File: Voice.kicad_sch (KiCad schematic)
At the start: 11 parts, among them Q401 MMBT3904, Q402 BSS84, U401 NE555D

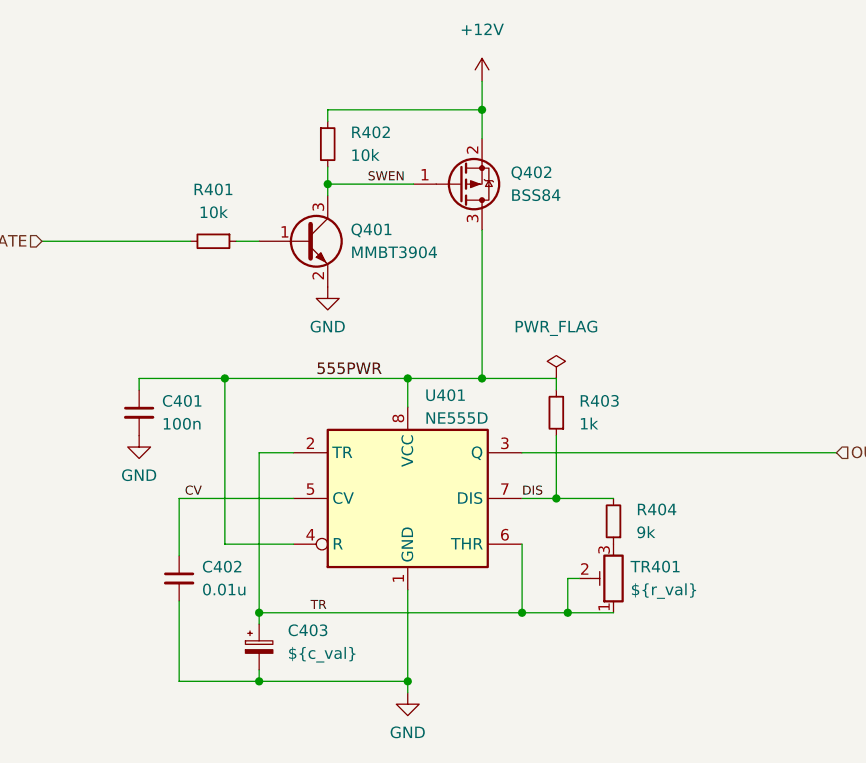
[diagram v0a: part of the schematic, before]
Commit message: swap to SMD Bourns 3224W, can stack in Eurorack now
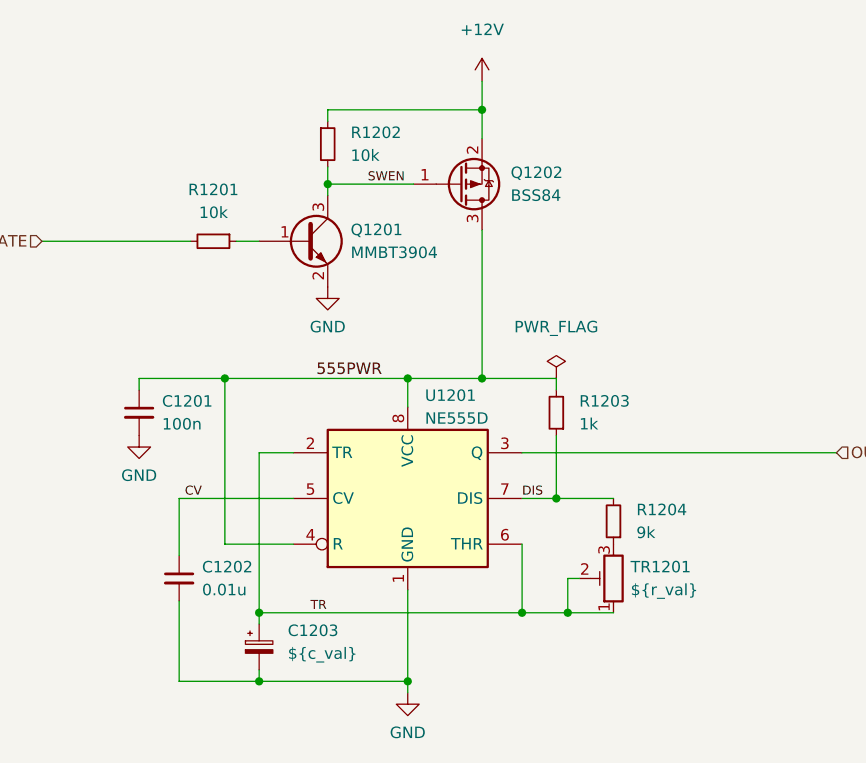
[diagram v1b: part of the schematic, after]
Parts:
- TR1201: renamed from TR401; footprint Potentiometer_THT:Potentiometer_Bourns_3296W_Vertical -> TripleFiveSynth:Potentiometer_Bourns_3224W_Vertical
- renumbered C401 to C1201, C402 to C1202, C403 to C1203, Q401 to Q1201, Q402 to Q1202, R401 to R1201, R402 to R1202, R403 to R1203, R404 to R1204, U401 to U1201
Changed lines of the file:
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@@
   (symbol (lib_id "Device:R_Potentiometer_Trim") (at 144.145 104.14 180)
     (in_bom yes) (on_board yes) (fields_autoplaced)
-    (property "Reference" "TR401" (id 0) (at 146.05 102.8699 0)
+    (property "Reference" "TR1201" (id 0) (at 146.05 102.8699 0)
       (effects (font (size 1.27 1.27)) (justify right))
     )
@@
       (effects (font (size 1.27 1.27)) (justify right))
     )
-    (property "Footprint" "Potentiometer_THT:Potentiometer_Bourns_3296W_Vertical" (id 2) (at 144.145 104.14 0)
+    (property "Footprint" "TripleFiveSynth:Potentiometer_Bourns_3224W_Vertical" (id 2) (at 144.145 104.14 0)
       (effects (font (size 1.27 1.27)) hide)
     )
@@
   (symbol (lib_id "Transistor_BJT:MMBT3904") (at 109.855 66.675 0)
     (in_bom yes) (on_board yes) (fields_autoplaced)
-    (property "Reference" "Q401" (id 0) (at 114.935 65.4049 0)
+    (property "Reference" "Q1201" (id 0) (at 114.935 65.4049 0)
       (effects (font (size 1.27 1.27)) (justify left))
     )
@@
   (symbol (lib_id "Timer:NE555D") (at 121.285 95.25 0)
     (in_bom yes) (on_board yes)
-    (property "Reference" "U401" (id 0) (at 123.19 83.82 0)
+    (property "Reference" "U1201" (id 0) (at 123.19 83.82 0)
       (effects (font (size 1.27 1.27)) (justify left))
     )
@@
   (symbol (lib_id "Device:C_Small") (at 95.885 104.14 0)
     (in_bom yes) (on_board yes) (fields_autoplaced)
-    (property "Reference" "C402" (id 0) (at 98.425 102.8762 0)
+    (property "Reference" "C1202" (id 0) (at 98.425 102.8762 0)
       (effects (font (size 1.27 1.27)) (justify left))
     )
@@
   (symbol (lib_id "Device:C_Small") (at 91.44 85.725 0)
     (in_bom yes) (on_board yes) (fields_autoplaced)
-    (property "Reference" "C401" (id 0) (at 93.98 84.4612 0)
+    (property "Reference" "C1201" (id 0) (at 93.98 84.4612 0)
       (effects (font (size 1.27 1.27)) (justify left))
     )
@@
   (symbol (lib_id "Device:R_Small") (at 137.795 85.725 180)
     (in_bom yes) (on_board yes) (fields_autoplaced)
-    (property "Reference" "R403" (id 0) (at 140.335 84.4549 0)
+    (property "Reference" "R1203" (id 0) (at 140.335 84.4549 0)
       (effects (font (size 1.27 1.27)) (justify right))
     )
@@
   (symbol (lib_id "Device:R_Small") (at 112.395 55.88 0)
     (in_bom yes) (on_board yes) (fields_autoplaced)
-    (property "Reference" "R402" (id 0) (at 114.935 54.6099 0)
+    (property "Reference" "R1202" (id 0) (at 114.935 54.6099 0)
       (effects (font (size 1.27 1.27)) (justify left))
     )
@@
   (symbol (lib_id "Device:R_Small") (at 99.695 66.675 270)
     (in_bom yes) (on_board yes) (fields_autoplaced)
-    (property "Reference" "R401" (id 0) (at 99.695 60.96 90))
+    (property "Reference" "R1201" (id 0) (at 99.695 60.96 90))
     (property "Value" "10k" (id 1) (at 99.695 63.5 90))
     (property "Footprint" "Resistor_SMD:R_0603_1608Metric" (id 2) (at 99.695 66.675 0)
@@
   (symbol (lib_id "Transistor_FET:BSS84") (at 127 60.325 0) (mirror x)
     (in_bom yes) (on_board yes) (fields_autoplaced)
-    (property "Reference" "Q402" (id 0) (at 132.715 59.0549 0)
+    (property "Reference" "Q1202" (id 0) (at 132.715 59.0549 0)
       (effects (font (size 1.27 1.27)) (justify left))
     )
@@
   (symbol (lib_id "Device:R_Small") (at 144.145 97.79 180)
     (in_bom yes) (on_board yes) (fields_autoplaced)
-    (property "Reference" "R404" (id 0) (at 146.685 96.5199 0)
+    (property "Reference" "R1204" (id 0) (at 146.685 96.5199 0)
       (effects (font (size 1.27 1.27)) (justify right))
     )
@@
   (symbol (lib_id "Device:C_Polarized_Small") (at 104.775 111.76 0)
     (in_bom yes) (on_board yes) (fields_autoplaced)
-    (property "Reference" "C403" (id 0) (at 107.95 109.9438 0)
-      (effects (font (size 1.27 1.27)) (justify left))
-    )
+    (property "Reference" "C1203" (id 0) (at 107.95 109.9438 0)
+      (effects (font (size 1.27 1.27)) (justify left))
+    )

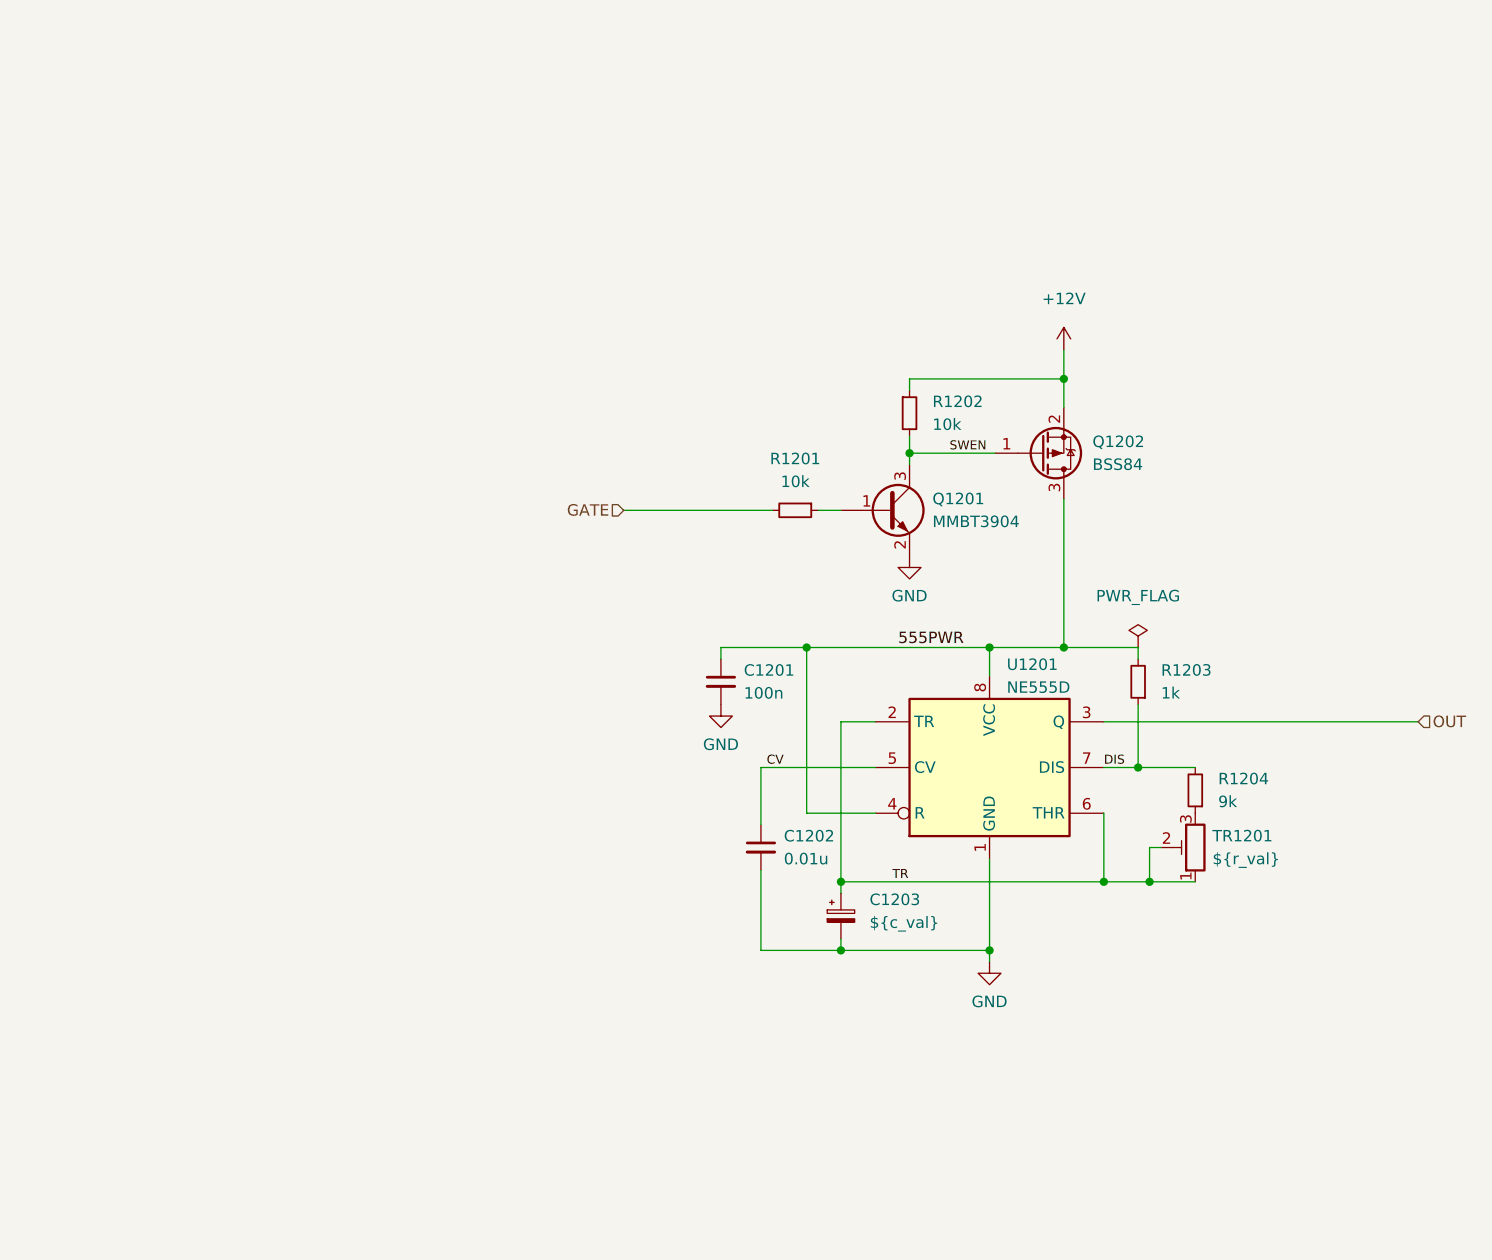
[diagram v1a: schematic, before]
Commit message: update with 5V and on-board sum
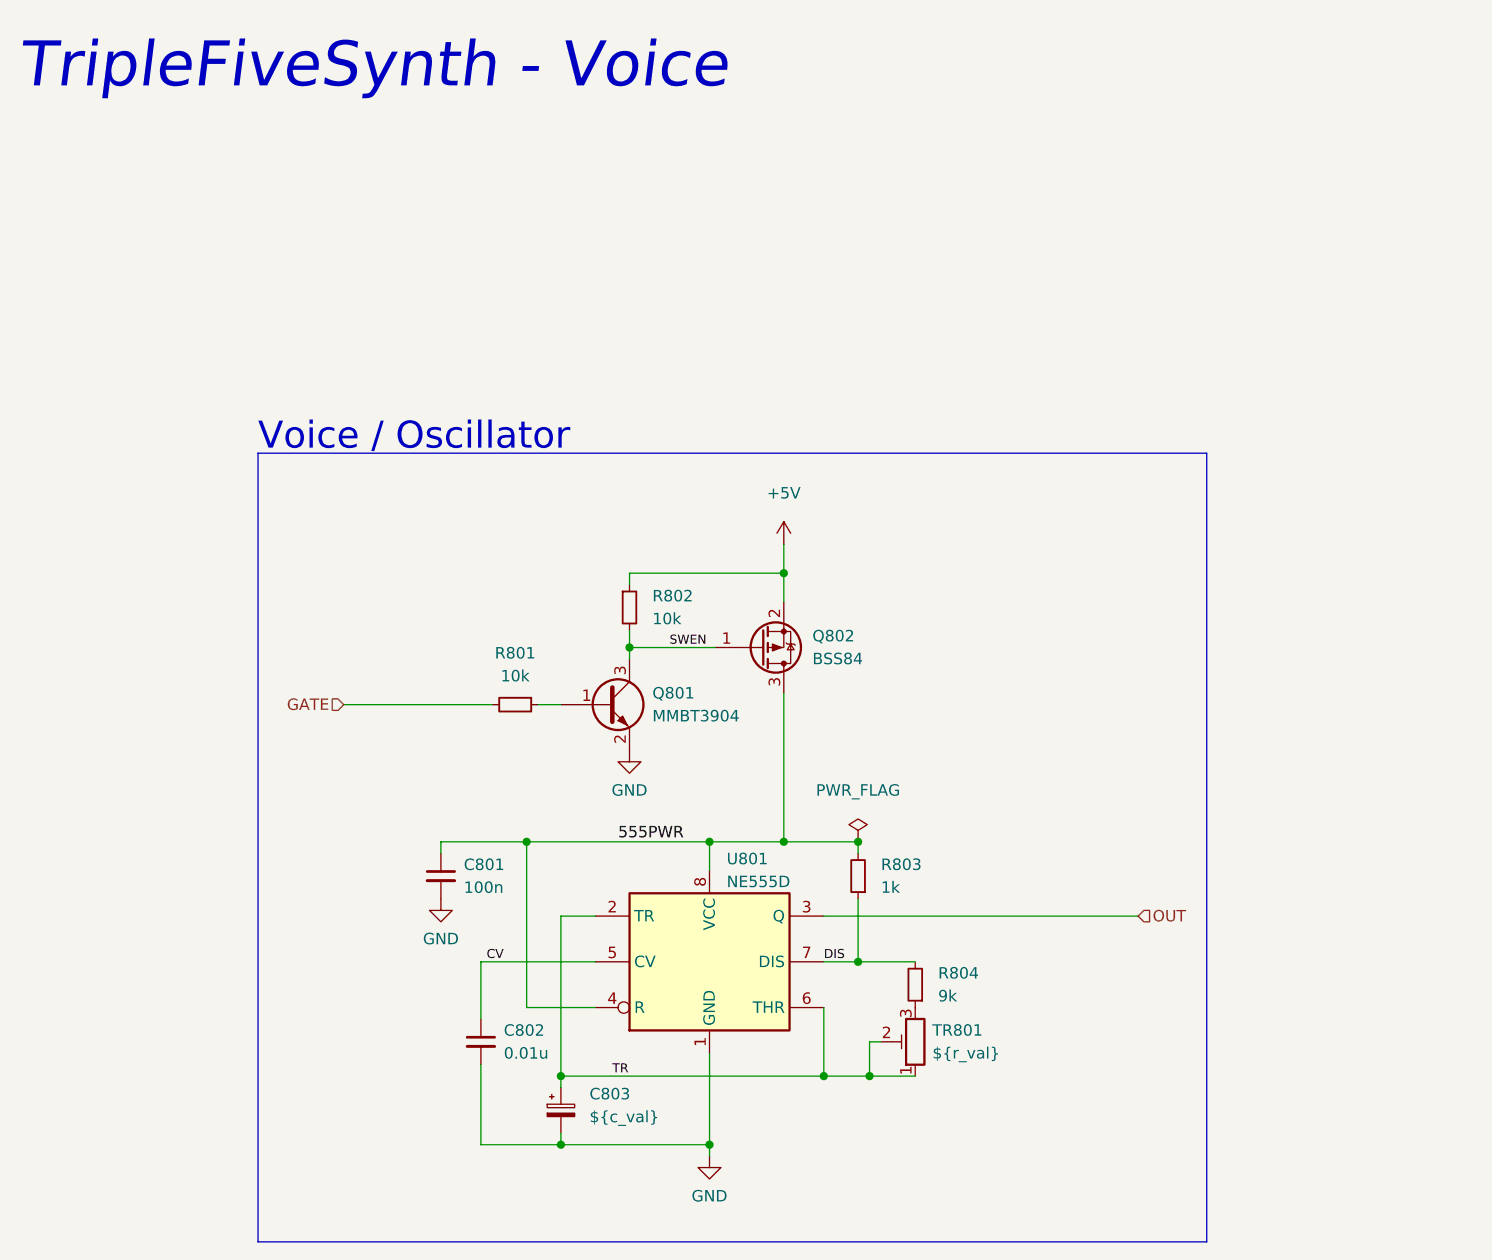
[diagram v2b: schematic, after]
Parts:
- renumbered C1201 to C801, C1202 to C802, C1203 to C803, Q1201 to Q801, Q1202 to Q802, R1201 to R801, R1202 to R802, R1203 to R803, R1204 to R804, TR1201 to TR801, U1201 to U801
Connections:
- net +12V renamed +5V
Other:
- note added: "TripleFiveSynth - Voice"
- note added: "Voice / Oscillator"
- company: (none) -> Alexander Brevig
- title: (none) -> TripleFiveSynth - Voice
- moved on the sheet: C801, C802, C803, Q801, Q802, R801, R802, R803, R804, TR801, U801
